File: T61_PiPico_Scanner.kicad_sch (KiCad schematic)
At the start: 18 parts, among them J101 GND, J102 VBUS, J103 EXT5V, J105 GND, J106 PWRSWITCH, U101 Pico

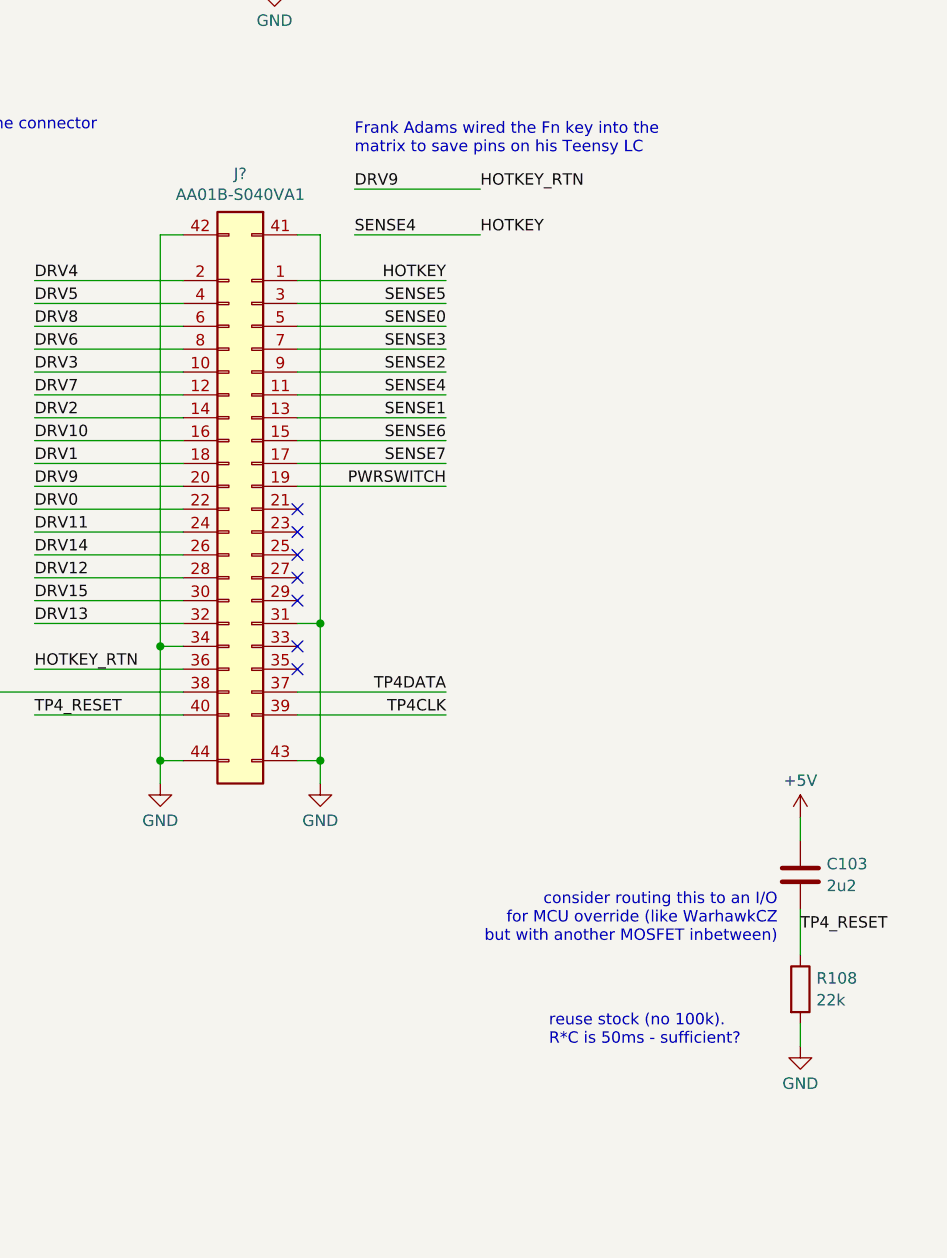
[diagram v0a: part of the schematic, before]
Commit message: version 1.2: reset IC; Molex 54363-0489
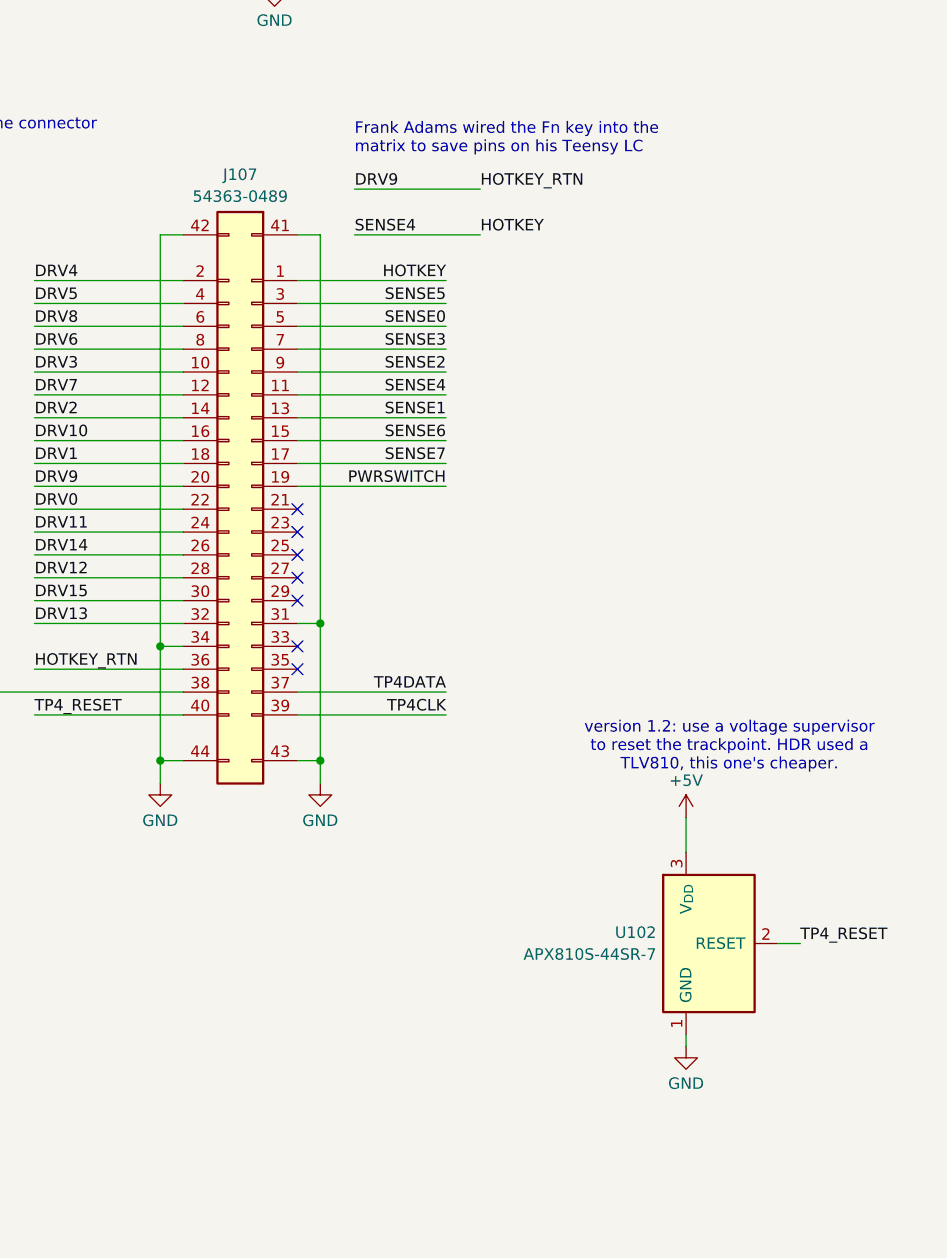
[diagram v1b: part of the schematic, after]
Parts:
- removed C103: 2u2, Capacitor_SMD:C_0603_1608Metric, symbol Device:C
- removed J?: AA01B-S040VA1, T61_Kb_Scanner:AA01B-S040VA1, symbol T61_Keyboard_by_WarhawkCZ:AA01B-S040VA1-jip_connectors
- removed R108: 22k, Resistor_SMD:R_0603_1608Metric, symbol Device:R
- added J107: 54363-0489, Molex_54363-0489:CON_543630489_var, symbol T61_Keyboard_by_WarhawkCZ:54363-0489
- added U102: APX810S-44SR-7, Package_TO_SOT_SMD:SOT-23, symbol Power_Supervisor:TLV810EA29DBZ
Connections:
- net +5V: now also J107.38, U102.3 (V_{DD})
- net DRV0: now also J107.22
- net DRV1: now also J107.18
- net DRV10: now also J107.16
- net DRV11: now also J107.24
- net DRV12: now also J107.28
- net DRV13: now also J107.32
- net DRV14: now also J107.26
- net DRV15: now also J107.30
- net DRV2: now also J107.14
- net DRV3: now also J107.10
- net DRV4: now also J107.2
- net DRV5: now also J107.4
- net DRV6: now also J107.8
- net DRV7: now also J107.12
- net DRV8: now also J107.6
- net DRV9: now also J107.20, J107.36
- net GND: now also J107.31, J107.34, J107.41, J107.42, J107.43, J107.44, U102.1 (GND)
- net HOTKEY: now also J107.1, J107.11
- net PWRSWITCH: now also J107.19
- net SENSE0: now also J107.5
- net SENSE1: now also J107.13
- net SENSE2: now also J107.9
- net SENSE3: now also J107.7
- net SENSE5: now also J107.3
- net SENSE6: now also J107.15
- net SENSE7: now also J107.17
- net TP4CLK: now also J107.39
- net TP4DATA: now also J107.37
- net TP4_RESET: now also J107.40, U102.2 (RESET)
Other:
- note added: "version 1.2: use a voltage supervisor to reset the trackpoint. HDR used a TLV810, this one's cheaper."
- note removed: "consider routing this to an I/O for MCU override (like WarhawkCZ but with another MOSFET inbetween)"
- note removed: "reuse stock (no 100k). R*C is 50ms - sufficient?"

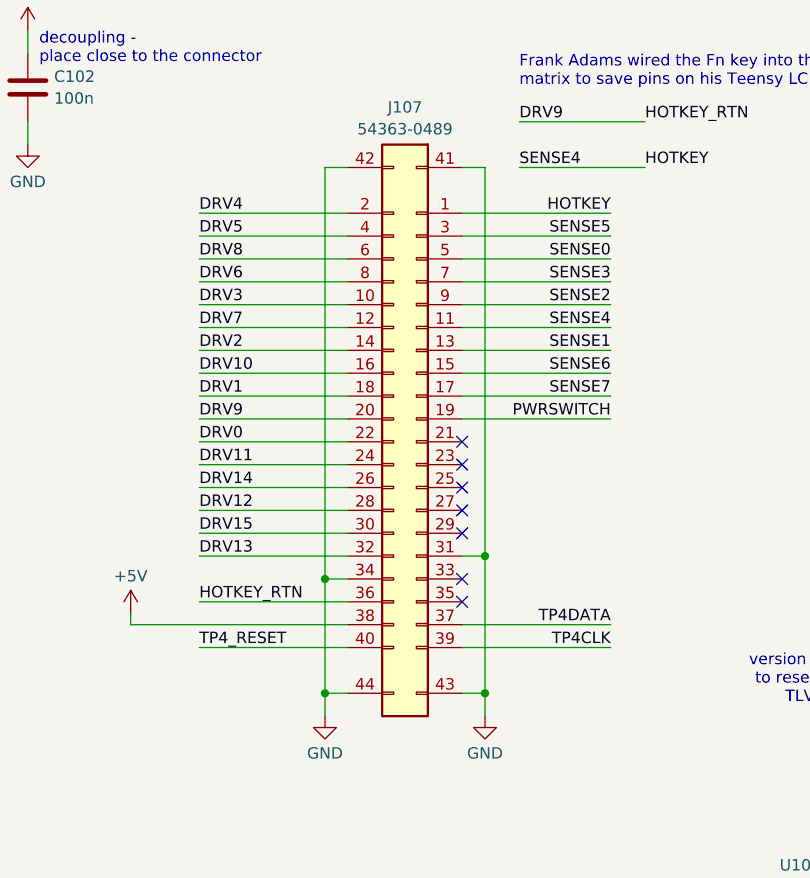
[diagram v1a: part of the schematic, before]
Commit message: version 2.0: use SMT version of Pi Pico
Now use two layers to allow keyboard connector and Pi Pico to both be on
the top side.

Mechanically incompatible (connector position / mounting holes) but
electrically identical to version 1, i.e. the (QMK) firmware can stay
the same.
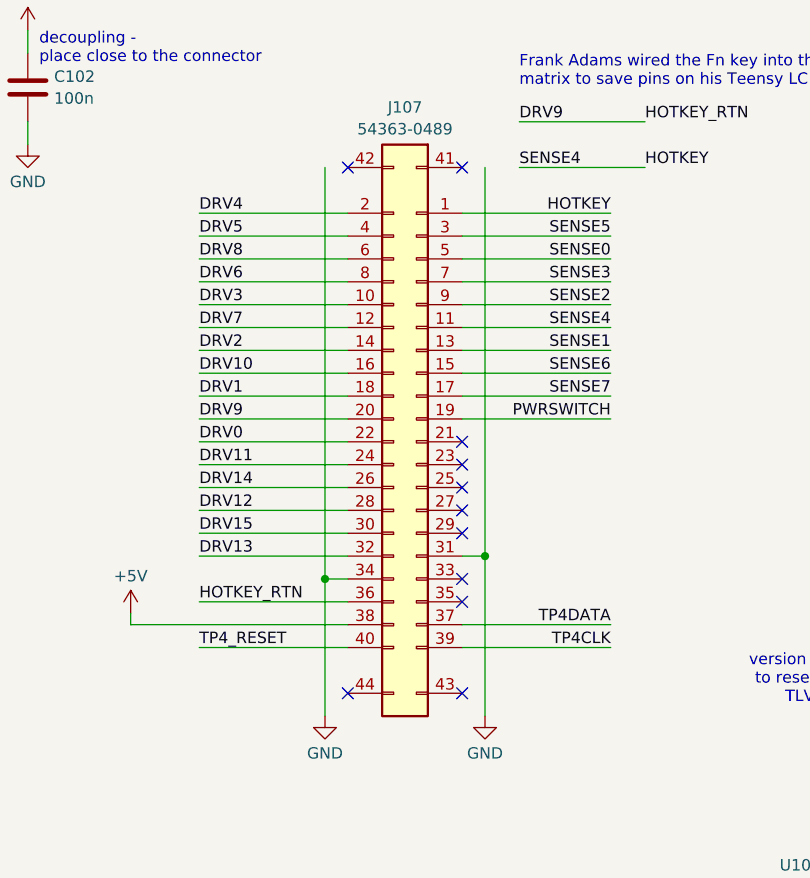
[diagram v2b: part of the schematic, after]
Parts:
- U101: footprint T61_Kb_Scanner:RPi_Pico_H -> MCU_RaspberryPi_and_Boards:RPi_Pico_SMD_TH
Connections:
- net GND: no longer J107.41, J107.42, J107.43, J107.44
- no-connect marks 13 -> 17
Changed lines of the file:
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@@
-	)
-	(junction
-		(at 217.17 123.19)
-		(diameter 0)
-		(color 0 0 0 0)
 	)
 	(junction
@@
 	)
 	(junction
-		(at 199.39 123.19)
-		(diameter 0)
-		(color 0 0 0 0)
-	)
-	(junction
 		(at 125.73 68.58)
 		(diameter 0)
@@
 	)
 	(no_connect
+		(at 201.93 123.19)
+	)
+	(no_connect
 		(at 88.9 121.92)
+	)
+	(no_connect
+		(at 201.93 64.77)
 	)
 	(no_connect
@@
 	)
 	(no_connect
+		(at 214.63 64.77)
+	)
+	(no_connect
 		(at 93.98 121.92)
 	)
@@
 		(at 214.63 102.87)
 	)
+	(no_connect
+		(at 214.63 123.19)
+	)
 	(wire
 		(pts
@@
 	(wire
 		(pts
-			(xy 217.17 64.77) (xy 214.63 64.77)
-		)
-		(stroke
-			(width 0)
-			(type default)
-		)
-	)
-	(wire
-		(pts
 			(xy 111.76 186.69) (xy 106.68 186.69)
 		)
@@
 	(wire
 		(pts
-			(xy 199.39 110.49) (xy 199.39 123.19)
+			(xy 199.39 110.49) (xy 199.39 125.73)
 		)
 		(stroke
@@
 	(wire
 		(pts
-			(xy 199.39 125.73) (xy 199.39 123.19)
-		)
-		(stroke
-			(width 0)
-			(type default)
-		)
-	)
-	(wire
-		(pts
 			(xy 125.73 50.8) (xy 116.84 50.8)
 		)
@@
 	(wire
 		(pts
-			(xy 217.17 125.73) (xy 217.17 123.19)
-		)
-		(stroke
-			(width 0)
-			(type default)
-		)
-	)
-	(wire
-		(pts
 			(xy 60.96 83.82) (xy 73.66 83.82)
 		)
@@
 	(wire
 		(pts
-			(xy 217.17 123.19) (xy 214.63 123.19)
-		)
-		(stroke
-			(width 0)
-			(type default)
-		)
-	)
-	(wire
-		(pts
 			(xy 214.63 72.39) (xy 231.14 72.39)
 		)
@@
 	(wire
 		(pts
-			(xy 199.39 123.19) (xy 201.93 123.19)
-		)
-		(stroke
-			(width 0)
-			(type default)
-		)
-	)
-	(wire
-		(pts
 			(xy 165.1 30.48) (xy 167.64 30.48)
 		)
@@
 	(wire
 		(pts
-			(xy 201.93 64.77) (xy 199.39 64.77)
-		)
-		(stroke
-			(width 0)
-			(type default)
-		)
-	)
-	(wire
-		(pts
 			(xy 60.96 68.58) (xy 73.66 68.58)
 		)
@@
 	(wire
 		(pts
-			(xy 217.17 123.19) (xy 217.17 107.95)
+			(xy 217.17 107.95) (xy 217.17 125.73)
 		)
 		(stroke
@@
 			)
 		)
-		(property "Footprint" "T61_Kb_Scanner:RPi_Pico_H"
+		(property "Footprint" "MCU_RaspberryPi_and_Boards:RPi_Pico_SMD_TH"
 			(at 91.44 92.71 90)
 			(effects
